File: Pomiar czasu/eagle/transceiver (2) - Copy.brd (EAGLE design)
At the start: 228.6 x 62.2 mm, 126 parts, among them IC1 MEGA8-AI, IC2 LF33, IC3 LF50, IC4 MEGA8-AI, IC5 LF33, IC6 LF50, U1 RFM69HW, U2 RFM69HW

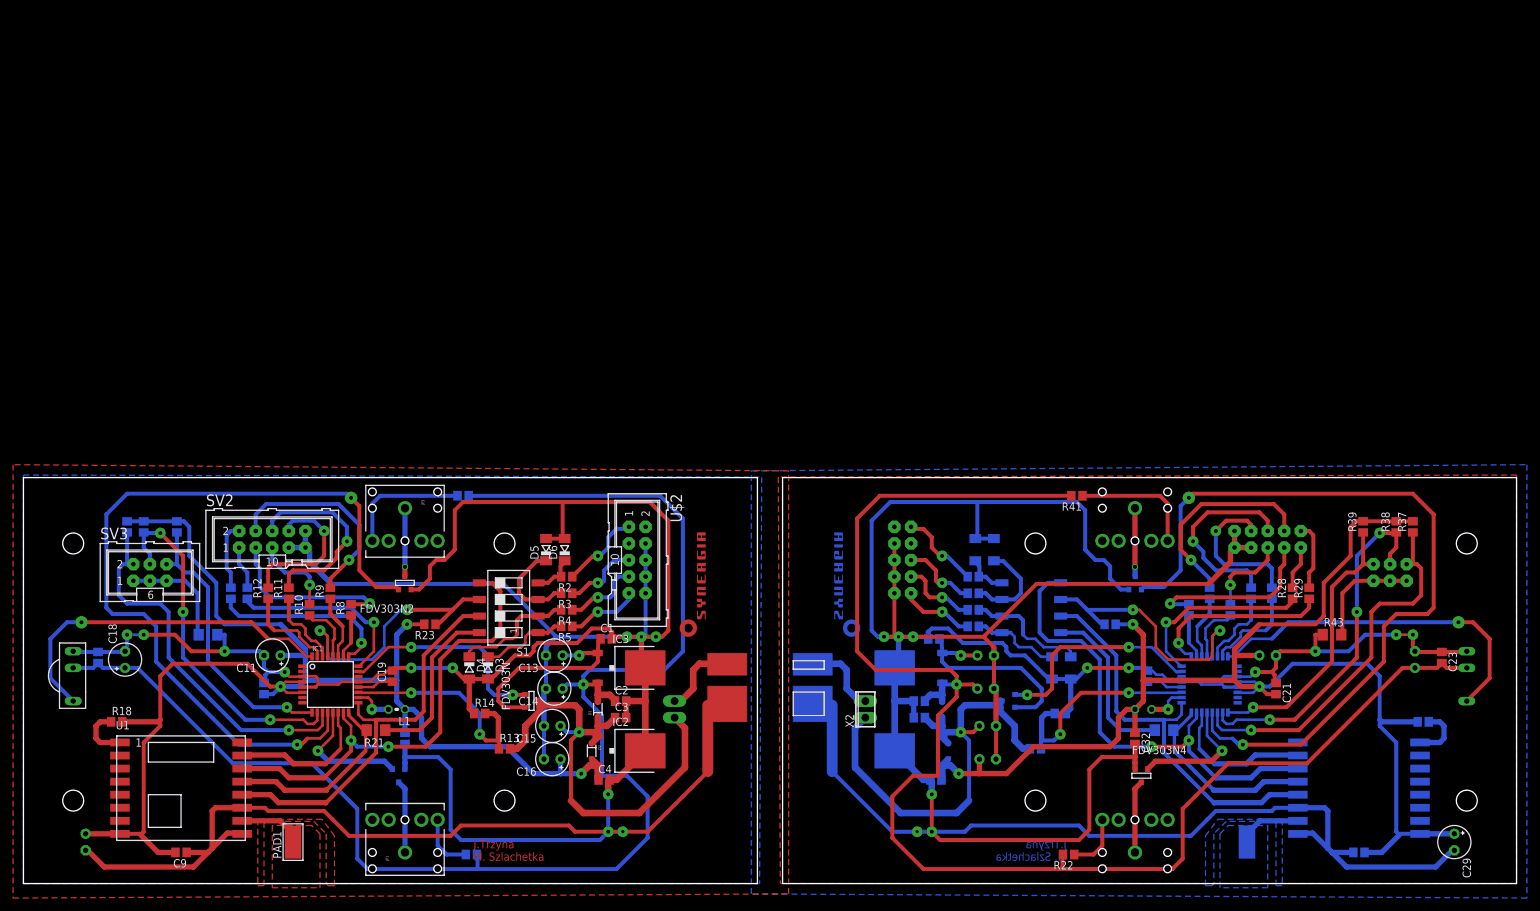
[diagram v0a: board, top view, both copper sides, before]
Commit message: RFM69:communication master->sensor works!
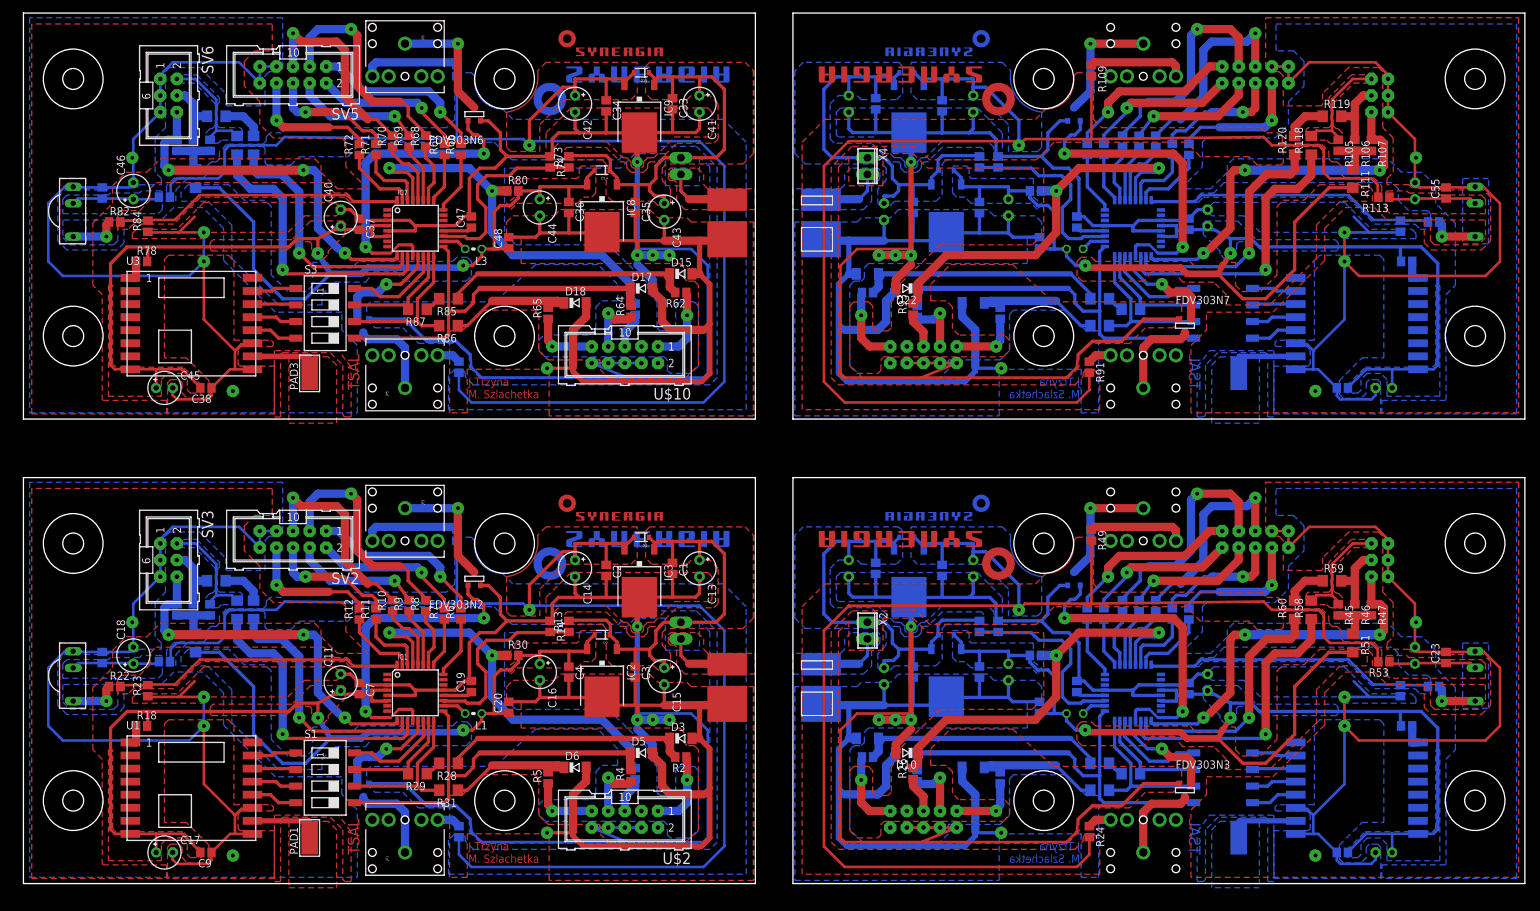
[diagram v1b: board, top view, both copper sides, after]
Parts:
- removed FDV303N: (no value), zetex:SOT-23
- added C33, C34, C35, C36, C37, C38, C39, C47, C48, C49, C50, C51, C52, C53, C54, C55, C63, C64: 100n, resistor:C0805
- added C40, C45, C56, C61: 22u, rcl:E2,5-5
- added C41, C42, C43, C44, C57, C58, C59, C60: 47u, rcl:E2,5-5
- added C46, C62: 4,7u, rcl:E2,5-5
- added D13, D14, D19, D20: BAS16HT1G, SparkFun:SOD-323
- added D15, D16, D17, D18, D21, D22, D23, D24: (no value), diode:SOD80C
- added FDV303N6, FDV303N7, FDV303N8: (no value), zetex:SOT-23
- added IC10, IC7: MEGA8-AI, atmel:TQFP32-08
- added IC11, IC8: LF33, linear:TO252
- added IC12, IC9: LF50, linear:TO252
- added JP5, JP6, JP7, JP8: (no value), SparkFun-Connectors:AUDIO-JACK
- added L3, L4: (no value), resistor:0204V
- added PAD3, PAD4: WIREPADSMD5-2,5, wirepad:5-2,5
- added R100, R102, R66, R67, R68, R69, R70, R72, R96, R97, R98, R99: 1.2k, resistor:R0805
- added R101, R71: 1,2k, resistor:R0805
- added R103, R105, R106, R107, R108, R110, R45, R46, R47, R48, R50, R73, R75, R76, R77, R78, R80: 10k, resistor:R0805
- added R104, R74: 3,6k, resistor:R0805
- added R109, R49, R79: (no value), resistor:R0805
- added R111, R115, R116, R117, R118, R119, R120, R51, R55, R56, R57, R58, R59, R60, R81, R85, R86, R87, R88, R89, R90: 0R, rcl:R1206
- added R112, R52, R62, R63, R64, R65, R82, R92, R93, R94, R95: 330k, resistor:R0805
- added R113, R53, R83: 220R, resistor:R0805
- added R114, R54, R84: 820k, resistor:R0805
- added R61, R91: 36,5R, resistor:R0805
- added S3, S4: SWS004, smd-special:SMS-004
- added SV5, SV7, U$10, U$14: (no value), con-harting-ml:ML10
- added SV6, SV8: (no value), con-harting-ml:ML6
- added TSOP2, TSOP3: TSOP1736, tsop:TSOP17XX
- added U$11, U$15, U$7: (no value), synergia_logo:SYNERGIA_16MM
- added U$12, U$16, U$8: (no value), synergia_logo:SYNERGIA_30MM
- added U$13, U$9: DEANS.MALE, bt_electromech:DEANSM
- added U3, U4: RFM69HW, SparkFun-RF:RFM69W-XXXS2
- added X3, X4: (no value), con-phoenix-254:2POL254
- C1, C10, C12, C19, C2, C20, C21, C22, C23, C3, C31, C32, C4, C5, C6, C7, C8, C9: value (none) -> 100n
- C11, C17, C24, C29: value (none) -> 22u
- C13, C14, C15, C16, C25, C26, C27, C28: value (none) -> 47u
- C18, C30: value (none) -> 4,7u
- D11, D12: value BAS16HT1G -> (none); device SparkFun:SOD-323 -> diode:SOD80C
- D7, D8: value (none) -> BAS16HT1G; device diode:SOD80C -> SparkFun:SOD-323
- R2, R25, R26, R27, R3, R4, R5: value (none) -> 330k
- R21: value 0R -> 220R; device rcl:R1206 -> resistor:R0805
- R22: value 36,5R -> 330k
- R23: value 1k -> 820k
- R24: value (none) -> 36,5R
- R28, R29, R31, R32: value 1.2k -> 0R; device resistor:R0805 -> rcl:R1206
- R30: value 1.2k -> 10k
- R33: value 1,2k -> 0R; device resistor:R0805 -> rcl:R1206
- R34: value 1.2k -> 330k
- R35: value 10k -> 0R; device resistor:R0805 -> rcl:R1206
- R36: value 3,6k -> 1.2k
- R37, R38, R39, R40: value 10k -> 1.2k
- R41: value (none) -> 1,2k
- R42: value 1k -> 1.2k
- R43: value 0R -> 10k; device rcl:R1206 -> resistor:R0805
- R44: value 0R -> 3,6k; device rcl:R1206 -> resistor:R0805
- U$4: value DEANS.MALE -> (none); device bt_electromech:DEANSM -> synergia_logo:SYNERGIA_30MM
- U$5: value (none) -> DEANS.MALE; device con-harting-ml:ML10 -> bt_electromech:DEANSM
- U$6: device synergia_logo:SYNERGIA_16MM -> con-harting-ml:ML10
- moved R33 158.4 mm to (29.5, 43.8), turned to 0 degrees
- moved R32 152.1 mm to (32.7, 39.4)
- moved R22 148.3 mm to (14.0, 27.6), turned to 0 degrees
- moved R29 139.3 mm to (60.3, 14.3), turned to 180 degrees
- moved R28 131.8 mm to (65.1, 15.9), turned to 180 degrees
- moved FDV303N5 124.5 mm to (52.1, 82.9), turned to 0 degrees
- moved R35 121.6 mm to (35.2, 39.4), turned to 90 degrees
- moved R31 120.4 mm to (65.1, 11.7), flipped to the top, turned to 180 degrees
- moved R30 103.7 mm to (74.9, 32.4), flipped to the top, turned to 0 degrees
- moved R43 54.0 mm to (146.4, 36.8), flipped to the bottom, turned to 90 degrees
- moved R34 50.3 mm to (149.5, 13.7)
- moved R37 49.2 mm to (165.4, 38.7), flipped to the bottom
- moved U$4 48.3 mm to (78.1, 51.4)
- moved R40 44.7 mm to (173.4, 40.0), turned to 90 degrees
- moved R23 44.4 mm to (19.1, 27.0), turned to 90 degrees
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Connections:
- removed net 5V_ENABLE: FDV303N.3, IC1.23
- removed net 5V_ENABLE1: FDV303N3.3, IC4.23
- removed net N$34: R27.1, U$5.9
- removed net N$43 (its old number): R31.2, SV1.4
- removed net N$44 (its old number): R32.2, SV1.5
- removed net N$45 (its old number): R33.2, SV1.6
- removed net N$53: JP2.TIP, R22.1
- new net +3V2: C36.1, C37.2, C38.2, C40.+, C44.+, C45.+, C48.1, D14.2, IC7.4, IC7.6, IC8.2, L3.1, R78.2, R80.2, R81.2, U3.8
- new net +3V4: C52.1, C53.2, C54.2, C56.+, C60.+, C61.+, C64.1, D20.2, IC10.4, IC10.6, IC11.2, L4.1, R108.2, R110.2, R111.2, U4.8
- new net +5V2: C34.1, C42.+, D13.2, IC9.2, R61.2, R79.2, R83.2
- new net +5V3: C50.1, C58.+, D19.2, IC12.2, R109.2, R113.2, R91.2
- new net ADC2: IC7.19, R73.1, R74.2
- new net ADC3: IC10.19, R103.1, R104.2
- new net GND2: C33.2, C34.2, C35.2, C36.2, C37.1, C38.1, C39.2, C40.-, C41.-, C42.-, C43.-, C44.-, C45.-, C46.-, C47.2, C48.2, D15.A, D16.A, D17.A, D18.A, FDV303N5.2, FDV303N6.2, IC7.21, IC7.3, IC7.5, IC8.3, IC9.3, R74.1, R84.1, SV5.10, SV5.7, SV5.9, SV6.1, SV6.3, SV6.5, TSOP2.GND, U$10.10, U$10.4, U$10.6, U$10.8, U$9.P$NEG, U3.11, U3.9
- new net GND3: C49.2, C50.2, C51.2, C52.2, C53.1, C54.1, C55.2, C56.-, C57.-, C58.-, C59.-, C60.-, C61.-, C62.-, C63.2, C64.2, D21.A, D22.A, D23.A, D24.A, FDV303N7.2, FDV303N8.2, IC10.21, IC10.3, IC10.5, IC11.3, IC12.3, R104.1, R114.1, SV7.10, SV7.7, SV7.9, SV8.1, SV8.3, SV8.5, TSOP3.GND, U$13.P$NEG, U$14.10, U$14.4, U$14.6, U$14.8, U4.11, U4.9
- new net LED11: IC7.24, R66.1
- new net LED12: IC7.25, R67.1
- new net LED13: IC7.26, R68.1
- new net LED14: IC7.27, R69.1
- new net LED15: IC7.28, R70.1
- new net LED16: IC10.24, R96.1
- new net LED17: IC10.25, R97.1
- new net LED18: IC10.26, R98.1
- new net LED19: IC10.27, R99.1
- new net LED20: IC10.28, R100.1
- new net LED_BATT_GR2: IC7.30, R71.1
- new net LED_BATT_GR3: IC10.30, R101.1
- new net LED_BATT_RED2: IC7.31, R72.1
- new net LED_BATT_RED3: IC10.31, R102.1
- new net LED_STRIPE2: FDV303N6.3, IC7.12
- new net LED_STRIPE3: FDV303N8.3, IC10.12
- new net MISO2: IC7.16, R86.2, S3.6
- new net MISO3: IC10.16, R116.2, S4.6
- new net MOSI2: IC7.15, R87.2, S3.7
- new net MOSI3: IC10.15, R117.2, S4.7
- new net N$100: R85.2, R87.1
- new net N$101: R75.1, R88.2, SV6.2
- new net N$102: R76.1, R89.2, SV6.4
- new net N$103: R89.1, R90.2
- new net N$105: S3.1, U3.15
- new net N$106: S3.2, U3.14
- new net N$107: S3.3, U3.13
- new net N$108: S3.4, U3.12
- new net N$109: R92.1, U$14.1
- new net N$110: R93.1, U$14.5
- new net N$111: R94.1, U$14.7
- new net N$112: R95.1, U$14.9
- new net N$113: R108.1, U4.1
- new net N$114: C49.1, C51.1, C57.+, C59.+, D19.1, D20.1, IC11.1, IC12.1, R103.2, X4.1
- new net N$115: IC10.18, L4.2
- new net N$116: C63.1, IC10.20
- new net N$117: PAD4.1, U4.10
- new net N$118: R96.2, SV7.1
- new net N$119: R97.2, SV7.2
- new net N$120: R98.2, SV7.3
- new net N$121: R99.2, SV7.4
- new net N$122: R100.2, SV7.5
- new net N$123: R101.2, SV7.6
- new net N$124: R102.2, SV7.8
- new net N$126: U$13.P$POS, X4.2
- new net N$127: JP7.TIP, R91.1
- new net N$128: FDV303N7.1, JP7.SLEEVE
- new net N$129: FDV303N8.1, JP8.SLEEVE
- new net N$130: JP8.TIP, R109.1
- new net N$131: R112.1, TSOP3.OUT
- new net N$132: C55.1, C62.+, R113.1, TSOP3.V+
- new net N$133: R105.2, R106.2, R107.2, R111.1
- new net N$134: D21.C, R115.1, R92.2
- new net N$135: D24.C, R116.1, R95.2
- new net N$136: R115.2, R117.1
- new net N$137: R105.1, R118.2, SV8.2
- new net N$138: R106.1, R119.2, SV8.4
- new net N$139: R119.1, R120.2
- new net N$141: S4.1, U4.15
- new net N$142: S4.2, U4.14
- new net N$143: S4.3, U4.13
- new net N$144: S4.4, U4.12
- new net N$37: S1.2, U1.14
- new net N$38: S1.4, U1.12
- new net N$39: S1.1, U1.15
- new net N$51: R41.2, SV1.6
- new net N$59: R52.1, TSOP1.OUT
- new net N$60: C23.1, C30.+, R53.1, TSOP1.V+
- new net N$61: R45.2, R46.2, R47.2, R51.1
- new net N$62: D9.C, R25.2, R55.1
- new net N$63: D12.C, R34.2, R56.1
- new net N$64: R55.2, R57.1
- new net N$65: R45.1, R58.2, SV4.2
- new net N$66: R46.1, R59.2, SV4.4
- new net N$67: R59.1, R60.2
- new net N$69: S2.1, U2.15
- new net N$70: S2.2, U2.14
- new net N$71: S2.3, U2.13
- new net N$72: S2.4, U2.12
- new net N$73: R62.1, U$10.1
- new net N$74: R63.1, U$10.5
- new net N$75: R64.1, U$10.7
- new net N$76: R65.1, U$10.9
- new net N$77: R78.1, U3.1
- new net N$78: C33.1, C35.1, C41.+, C43.+, D13.1, D14.1, IC8.1, IC9.1, R73.2, X3.1
- new net N$79: IC7.18, L3.2
- new net N$80: C47.1, IC7.20
- new net N$81: PAD3.1, U3.10
- new net N$82: R66.2, SV5.1
- new net N$83: R67.2, SV5.2
- new net N$84: R68.2, SV5.3
- new net N$85: R69.2, SV5.4
- new net N$86: R70.2, SV5.5
- new net N$87: R71.2, SV5.6
- new net N$88: R72.2, SV5.8
- new net N$90: U$9.P$POS, X3.2
- new net N$91: JP5.TIP, R61.1
- new net N$92: FDV303N5.1, JP5.SLEEVE
- new net N$93: FDV303N6.1, JP6.SLEEVE
- new net N$94: JP6.TIP, R79.1
- new net N$95: R82.1, TSOP2.OUT
- new net N$96: C39.1, C46.+, R83.1, TSOP2.V+
- new net N$97: R75.2, R76.2, R77.2, R81.1
- new net N$98: D15.C, R62.2, R85.1
- new net N$99: D18.C, R65.2, R86.1
- new net RESET2: D16.C, IC7.29, R63.2, R80.1
- new net RESET3: D22.C, IC10.29, R110.1, R93.2
- new net SCK2: D17.C, IC7.17, R64.2, S3.5
- new net SCK3: D23.C, IC10.17, R94.2, S4.5
- new net SS2: IC7.14, S3.8
- new net SS3: IC10.14, S4.8
- new net SWITCH_DOWN2: IC7.11, R88.1
- new net SWITCH_DOWN3: IC10.11, R118.1
- new net SWITCH_OK2: IC7.10, R90.1
- new net SWITCH_OK3: IC10.10, R120.1
- new net SWITCH_UP2: IC7.9, R77.1, SV6.6
- new net SWITCH_UP3: IC10.9, R107.1, SV8.6
- new net TSAL_ENABLE2: FDV303N5.3, IC7.13
- new net TSAL_ENABLE3: FDV303N7.3, IC10.13
- new net TSOP_OUT2: IC7.32, R82.2, R84.2
- new net TSOP_OUT3: IC10.32, R112.2, R114.2
- net +3V1: now also D8.2, R48.2, R50.2, R51.2; no longer D12.2, R37.2, R38.2, R39.2, R40.2, R42.2
- net +3V3: now also R20.2, R30.2; no longer R15.2, R16.2, R17.2, R23.2
- net +5V: now also R21.2; no longer C10.2, C18.+, TSOP.V+
- net +5V1: now also D7.2, R24.2, R49.2, R53.2; no longer C23.2, C30.+, D11.2, R22.2, R41.2, TSOP1.V+
- net ADC1: now also R43.1, R44.2; no longer R35.1, R36.2
- net GND: now also C10.2, R23.1, SV3.1, SV3.3, SV3.5; no longer C10.1, R20.1
- net GND1: now also C23.2, D11.A, D12.A, FDV303N3.2, R44.1, R54.1, SV4.1, SV4.3, SV4.5, U$5.P$NEG, U$6.10, U$6.4, U$6.6, U$6.8; no longer C23.1, D7.A, D8.A, FDV303N5.2, R36.1, R43.1, U$4.P$NEG, U$5.10, U$5.4, U$5.6, U$5.8
- net LED10: now also R40.1; no longer R32.1
- net LED6: now also R36.1; no longer R28.1
- net LED7: now also R37.1; no longer R29.1
- net LED8: now also R38.1; no longer R30.1
- net LED9: now also R39.1; no longer R31.1
- net LED_BATT_GR1: now also R41.1; no longer R33.1
- net LED_BATT_RED1: now also R42.1; no longer R34.1
- net LED_STRIPE1: now also FDV303N4.3; no longer FDV303N5.3
- net MISO: now also R31.2, S1.6; no longer R21.2, U1.13
- net MISO1: now also R56.2, S2.6; no longer R44.2, U2.13
- net MOSI: now also R29.2, S1.7; no longer S1.5, U1.14
- net MOSI1: now also R57.2, S2.7; no longer S2.5, U2.14
- net N$1: now also R22.1, TSOP.OUT; no longer C1.1, C13.+, FDV303N.2, IC3.1
- net N$22: now also R26.1, U$6.5; no longer R24.1, U$5.1
- net N$23: now also R15.2, R16.2, R17.2, R20.1; no longer R20.2, SV3.1, SV3.3, SV3.5
- net N$24: now also R27.1, U$6.7; no longer R21.1, S1.8
- net N$25: now also C10.1, C18.+, R21.1, TSOP.V+; no longer R25.1, U$5.5
- net N$27: now also C1.1, C13.+, IC3.1; no longer FDV303N.1
- net N$29: now also R28.2, R29.1; no longer D6.C, R2.2, S1.4
- net N$3: now also R25.1, U$6.1; no longer C25.+, C5.1, FDV303N3.2, IC6.1
- net N$30: now also D3.C, R2.2, R28.1; no longer D5.C, R3.2, S1.3
- net N$31: now also D6.C, R31.1, R5.2; no longer D4.C, R4.2, S1.2
- net N$32: now also R15.1, R32.2, SV3.2; no longer D3.C, R5.2, S1.1
- net N$33: now also R16.1, R33.2, SV3.4; no longer R26.1, U$5.7
- net N$35: now also R33.1, R35.2; no longer R40.1, U2.1
- net N$36: now also S1.3, U1.13; no longer C27.+, C8.1, D11.1, D12.1, FDV303N3.1, IC5.1, R35.2, X2.1
- net N$40: now also R34.1, U$6.9; no longer R28.2, SV1.1
- net N$41: now also R48.1, U2.1; no longer R29.2, SV1.2
- net N$42: now also C25.+, C27.+, C5.1, C8.1, D7.1, D8.1, IC5.1, IC6.1, R43.2, X2.1; no longer R30.2, SV1.3
- net N$46: now also R36.2, SV1.1; no longer R34.2, SV1.8
- net N$47: now also R37.2, SV1.2; no longer D8.C, R24.2, S2.4
- net N$48: now also R38.2, SV1.3; no longer D7.C, R25.2, S2.3
- net N$49: now also R39.2, SV1.4; no longer D10.C, R26.2, S2.2
- net N$50: now also R40.2, SV1.5; no longer D9.C, R27.2, S2.1
- net N$52: now also R42.2, SV1.8; no longer U$4.P$POS, X2.2
- net N$54: now also U$5.P$POS, X2.2; no longer FDV303N4.1, JP2.SLEEVE
- net N$55: now also JP2.TIP, R24.1; no longer FDV303N5.1, JP4.SLEEVE
- net N$56: now also FDV303N3.1, JP2.SLEEVE; no longer JP4.TIP, R41.1
- net N$57: now also FDV303N4.1, JP4.SLEEVE; no longer R43.2, SV4.1, SV4.3, SV4.5
- net N$58: now also JP4.TIP, R49.1; no longer R44.1, S2.8
- net RESET: now also D4.C, R3.2, R30.1; no longer R23.1, S1.6
- net RESET1: now also D10.C, R26.2, R50.1; no longer R42.1, S2.6
- net SCK: now also D5.C, R4.2, S1.5; no longer S1.7, U1.12
- net SCK1: now also D11.C, R27.2, S2.5; no longer S2.7, U2.12
- net SS: now also S1.8; no longer U1.15
- net SS1: now also S2.8; no longer U2.15
- net SWITCH_DOWN: now also R32.1; no longer R15.1, SV3.2
- net SWITCH_DOWN1: now also R58.1; no longer R37.1, SV4.2
- net SWITCH_OK: now also R35.1; no longer R16.1, SV3.4
- net SWITCH_OK1: now also R60.1; no longer R38.1, SV4.4
- net SWITCH_UP1: now also R47.1; no longer R39.1
- net TSAL_ENABLE1: now also FDV303N3.3; no longer FDV303N4.3
- net TSOP_OUT: now also R22.2, R23.2; no longer TSOP.OUT
- net TSOP_OUT1: now also R52.2, R54.2; no longer TSOP1.OUT
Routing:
- net GND2: track 0.00 -> 489.9 mm, vias 0 -> 9
- net GND3: track 0.00 -> 489.9 mm, vias 0 -> 9
- net +5V2: track 0.00 -> 212.4 mm, vias 0 -> 1
- net +5V3: track 0.00 -> 212.4 mm, vias 0 -> 1
- net +3V4: track 0.00 -> 184.0 mm, vias 0 -> 2
- net +3V2: track 0.00 -> 184.0 mm, vias 0 -> 2
- net LED_STRIPE1: track 121.6 -> 47.7 mm
- net LED_STRIPE: track 121.6 -> 47.7 mm
- net N$78: track 0.00 -> 68.1 mm
- net N$114: track 0.00 -> 68.1 mm
- net N$36: track 74.6 -> 6.92 mm, vias 1 -> 0
- net RESET3: track 0.00 -> 61.3 mm, vias 0 -> 2
- net RESET2: track 0.00 -> 61.3 mm, vias 0 -> 2
- net SCK3: track 0.00 -> 61.1 mm
- net SCK2: track 0.00 -> 61.1 mm
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- added copper zone on layer 1, net +3V1
- added copper zone on layer 16, net +3V1
- added copper zone on layer 1, net +3V2
- added copper zone on layer 16, net +3V2
- added copper zone on layer 1, net +3V3
- added copper zone on layer 16, net +3V3
- added copper zone on layer 1, net +3V4
- added copper zone on layer 16, net +3V4
- added copper zone on layer 1, net +5V
- added copper zone on layer 16, net +5V
- added copper zone on layer 1, net +5V1
- added copper zone on layer 16, net +5V1
- added copper zone on layer 1, net +5V2
- added copper zone on layer 16, net +5V2
- added copper zone on layer 1, net +5V3
- added copper zone on layer 16, net +5V3
- added copper zone on layer 1, net GND2
- added copper zone on layer 16, net GND2
- added copper zone on layer 1, net GND3
- added copper zone on layer 16, net GND3
- added copper zone on layer 16, net N$1
- added copper zone on layer 16, net N$101
- added copper zone on layer 1, net N$104
- added copper zone on layer 16, net N$114
- added copper zone on layer 16, net N$117
- added copper zone on layer 16, net N$125
- added copper zone on layer 16, net N$126
- added copper zone on layer 1, net N$131
- added copper zone on layer 1, net N$132
- added copper zone on layer 1, net N$137
- added copper zone on layer 16, net N$140
- added copper zone on layer 1, net N$19
- added copper zone on layer 16, net N$25
- added copper zone on layer 1, net N$27
- added copper zone on layer 16, net N$32
- added copper zone on layer 1, net N$34
- added copper zone on layer 16, net N$42
- added copper zone on layer 16, net N$53
- added copper zone on layer 16, net N$54
- added copper zone on layer 1, net N$59
- added copper zone on layer 1, net N$60
- added copper zone on layer 1, net N$65
- added copper zone on layer 16, net N$68
- added copper zone on layer 1, net N$78
- added copper zone on layer 1, net N$81
- added copper zone on layer 1, net N$89
- added copper zone on layer 1, net N$90
- added copper zone on layer 16, net N$95
- added copper zone on layer 16, net N$96
- added copper zone on layer 1, net TSOP_OUT
- added copper zone on layer 16, net TSOP_OUT1
- added copper zone on layer 1, net TSOP_OUT2
- added copper zone on layer 16, net TSOP_OUT3
- removed copper zone on layer 16, net N$51
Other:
- board size 228.6 x 62.2 mm -> 229.9 x 133.3 mm
- board text added: "TSAL"

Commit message: Channel: 442MHz(!!), ping with acknowledgement
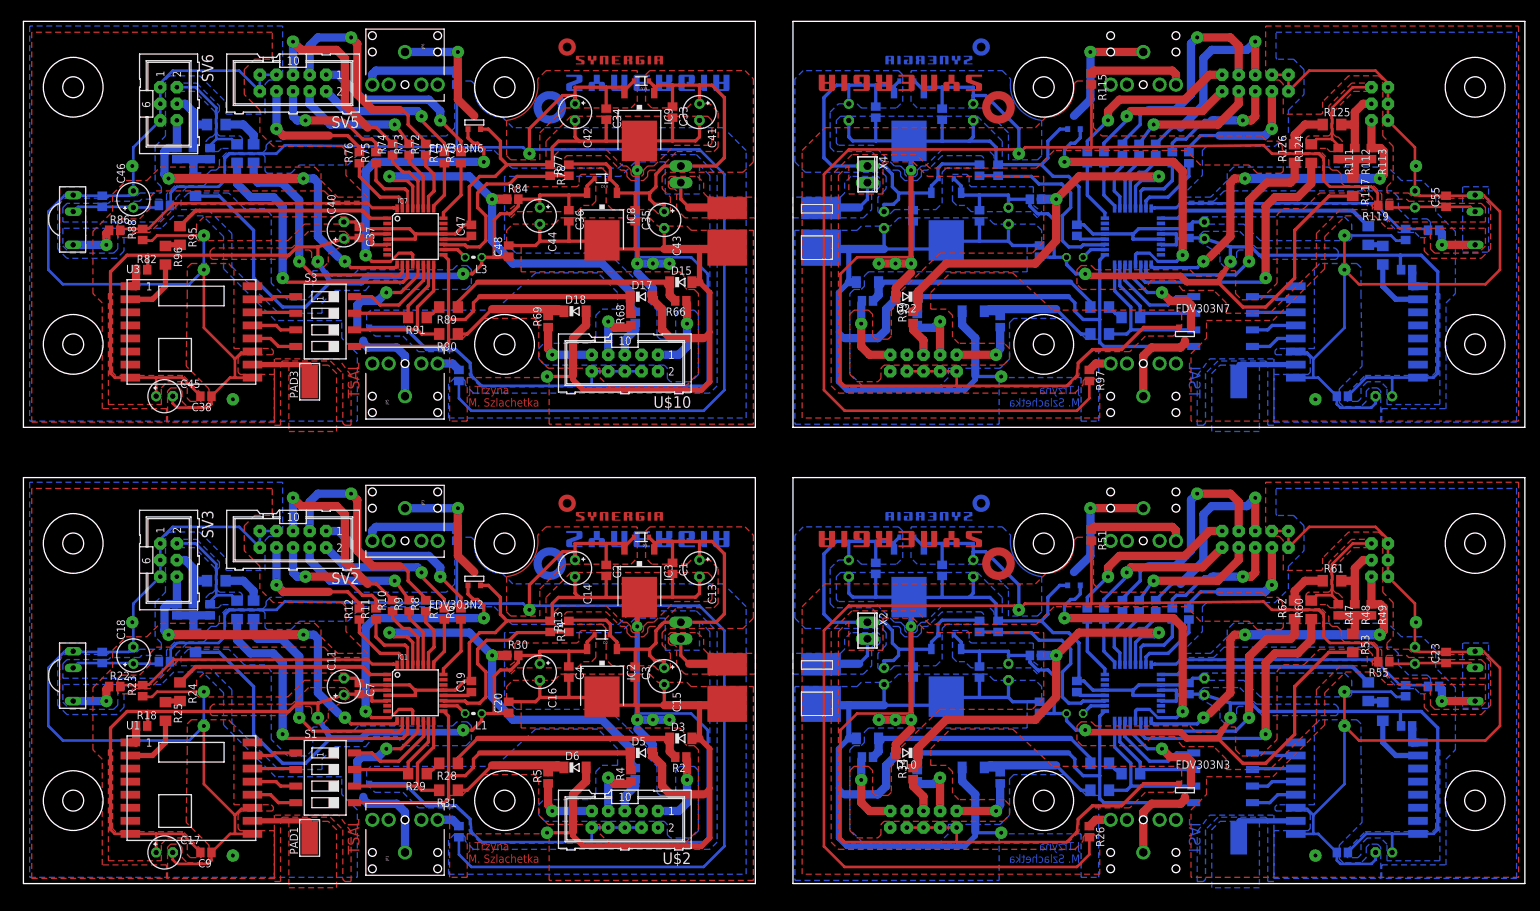
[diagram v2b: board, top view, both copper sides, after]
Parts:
- added R121, R122, R123, R124, R125, R126, R127, R128: 0R, rcl:R1206
- R100, R36, R37, R66, R67, R68, R69, R98, R99: value 1.2k -> 330k
- R101: value 1,2k -> 330k
- R103, R105, R106, R108, R73, R76: value 10k -> 1.2k
- R104, R44, R74: value 3,6k -> 1.2k
- R107, R43, R75: value 10k -> 1,2k
- R109, R49, R79: value (none) -> 10k
- R110, R46, R78: value 10k -> 3,6k
- R111, R116, R81: value 0R -> 10k; device rcl:R1206 -> resistor:R0805
- R112, R52, R82: value 330k -> 10k
- R113: value 220R -> 10k
- R114, R84: value 820k -> 10k
- R115, R51: value 0R -> (none); device rcl:R1206 -> resistor:R0805
- R118, R86: value 0R -> 330k; device rcl:R1206 -> resistor:R0805
- R119, R55, R87: value 0R -> 220R; device rcl:R1206 -> resistor:R0805
- R120, R56, R88: value 0R -> 820k; device rcl:R1206 -> resistor:R0805
- R24, R61, R91: value 36,5R -> 0R; device resistor:R0805 -> rcl:R1206
- R25, R62, R63, R64, R92, R93, R94, R95: value 330k -> 0R; device resistor:R0805 -> rcl:R1206
- R26, R65: value 330k -> 36,5R
- R41, R71: value 1,2k -> 1.2k
- R53: value 220R -> 0R; device resistor:R0805 -> rcl:R1206
- R54: value 820k -> 330k
- R83: value 220R -> (none)
- R96: value 1.2k -> 0R; device resistor:R0805 -> rcl:R1206
- R97: value 1.2k -> 36,5R
- moved R96 142.1 mm to (21.7, 93.7), flipped to the top, turned to 270 degrees
- moved R24 140.9 mm to (24.0, 26.8)
- moved R61 137.6 mm to (200.3, 43.8), flipped to the top, turned to 0 degrees
- moved R64 130.4 mm to (208.1, 23.8), flipped to the bottom, turned to 270 degrees
- moved R63 126.6 mm to (205.9, 26.8), turned to 270 degrees
- moved R95 126.1 mm to (24.0, 96.7), flipped to the top, turned to 270 degrees
- moved R93 110.4 mm to (29.5, 113.7), flipped to the bottom, turned to 0 degrees
- moved R25 107.7 mm to (21.7, 23.8), flipped to the top, turned to 270 degrees
- moved R62 105.8 mm to (194.6, 39.4), turned to 90 degrees
- moved R94 104.4 mm to (35.2, 109.2)
- moved R91 103.2 mm to (60.3, 84.1), turned to 180 degrees
- moved R92 98.8 mm to (32.7, 109.2), turned to 90 degrees
- moved R78 64.1 mm to (80.6, 106.7), turned to 270 degrees
- moved R52 61.1 mm to (154.9, 32.4)
- moved R77 60.1 mm to (83.5, 106.7), flipped to the top, turned to 90 degrees
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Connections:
- removed net N$109 (its old number): R92.1, U$14.1
- removed net N$110 (its old number): R93.1, U$14.5
- removed net N$111 (its old number): R94.1, U$14.7
- removed net N$112 (its old number): R95.1, U$14.9
- removed net N$121 (its old number): R99.2, SV7.4
- removed net N$122 (its old number): R100.2, SV7.5
- removed net N$123 (its old number): R101.2, SV7.6
- removed net N$131: R112.1, TSOP3.OUT
- removed net N$132 (its old number): C55.1, C62.+, R113.1, TSOP3.V+
- removed net N$134 (its old number): D21.C, R115.1, R92.2
- removed net N$135 (its old number): D24.C, R116.1, R95.2
- removed net N$46 (its old number): R36.2, SV1.1
- removed net N$47 (its old number): R37.2, SV1.2
- removed net N$55: JP2.TIP, R24.1
- removed net N$58 (its old number): JP4.TIP, R49.1
- removed net N$59 (its old number): R52.1, TSOP1.OUT
- removed net N$73 (its old number): R62.1, U$10.1
- removed net N$74 (its old number): R63.1, U$10.5
- removed net N$83 (its old number): R67.2, SV5.2
- removed net N$84 (its old number): R68.2, SV5.3
- removed net N$85 (its old number): R69.2, SV5.4
- removed net N$94 (its old number): JP6.TIP, R79.1
- removed net N$96 (its old number): C39.1, C46.+, R83.1, TSOP2.V+
- removed net N$97 (its old number): R75.2, R76.2, R77.2, R81.1
- new net DIO0: IC1.1, R24.1
- new net DIO1: IC4.1, R63.1
- new net DIO2: IC7.1, R95.1
- new net DIO3: IC10.1, R127.1
- new net N$104: R89.2, R91.1
- new net N$105: R79.1, R92.2, SV6.2
- new net N$106: R80.1, R93.2, SV6.4
- new net N$107: R93.1, R94.2
- new net N$115: R98.1, U$14.1
- new net N$116: R99.1, U$14.5
- new net N$117: R100.1, U$14.7
- new net N$125: R103.2, SV7.2
- new net N$126: R104.2, SV7.3
- new net N$128: R106.2, SV7.5
- new net N$129: R107.2, SV7.6
- new net N$140: D21.C, R121.1, R98.2
- new net N$141: D24.C, R101.2, R122.1
- new net N$142: R121.2, R123.1
- new net N$143: R111.1, R124.2, SV8.2
- new net N$144: R112.1, R125.2, SV8.4
- new net N$145: R125.1, R126.2
- new net N$151: R127.2, R128.1
- new net N$152: R128.2, U4.2
- new net N$43: C25.+, C27.+, C5.1, C8.1, D7.1, D8.1, IC5.1, IC6.1, R45.2, X2.1
- new net N$45: R25.2, U1.2
- new net N$53: R43.2, SV1.6
- new net N$54: R44.2, SV1.8
- new net N$57: JP2.TIP, R26.1
- new net N$68: R48.1, R61.2, SV4.4
- new net N$69: R61.1, R62.2
- new net N$79: R68.1, U$10.7
- new net N$80: R69.1, U$10.9
- new net N$81: R82.1, U3.1
- new net N$89: R73.2, SV5.4
- new net N$90: R74.2, SV5.5
- new net N$92: R76.2, SV5.8
- net +3V1: now also R52.2, R53.2; no longer R48.2, R51.2
- net +3V2: now also R82.2, R84.2, R85.2; no longer R78.2, R80.2, R81.2
- net +3V4: now also R114.2, R116.2, R117.2; no longer R108.2, R110.2, R111.2
- net +5V1: now also R26.2, R51.2, R55.2; no longer R24.2, R49.2, R53.2
- net +5V2: now also R65.2, R87.2; no longer R61.2, R79.2
- net +5V3: now also R115.2, R119.2, R97.2; no longer R109.2, R113.2, R91.2
- net ADC1: now also R45.1, R46.2; no longer R43.1, R44.2
- net ADC2: now also R77.1, R78.2; no longer R73.1, R74.2
- net ADC3: now also R109.1, R110.2; no longer R103.1, R104.2
- net GND1: now also R46.1, R56.1; no longer R44.1, R54.1
- net GND2: now also R78.1, R88.1; no longer R74.1, R84.1
- net GND3: now also R110.1, R120.1; no longer R104.1, R114.1
- net LED10: now also R42.1; no longer R40.1
- net LED11: now also R70.1; no longer R66.1
- net LED12: now also R71.1; no longer R67.1
- net LED13: now also R72.1; no longer R68.1
- net LED14: now also R73.1; no longer R69.1
- net LED15: now also R74.1; no longer R70.1
- net LED16: now also R102.1; no longer R96.1
- net LED17: now also R103.1; no longer R97.1
- net LED18: now also R104.1; no longer R98.1
- net LED19: now also R105.1; no longer R99.1
- net LED20: now also R106.1; no longer R100.1
- net LED6: now also R38.1; no longer R36.1
- net LED7: now also R39.1; no longer R37.1
- net LED8: now also R40.1; no longer R38.1
- net LED9: now also R41.1; no longer R39.1
- net LED_BATT_GR1: now also R43.1; no longer R41.1
- net LED_BATT_GR2: now also R75.1; no longer R71.1
- net LED_BATT_GR3: now also R107.1; no longer R101.1
- net LED_BATT_RED1: now also R44.1; no longer R42.1
- net LED_BATT_RED2: now also R76.1; no longer R72.1
- net LED_BATT_RED3: now also R108.1; no longer R102.1
- net MISO1: now also R58.2; no longer R56.2
- net MISO2: now also R90.2; no longer R86.2
- net MISO3: now also R122.2; no longer R116.2
- net MOSI1: now also R59.2; no longer R57.2
- net MOSI2: now also R91.2; no longer R87.2
- net MOSI3: now also R123.2; no longer R117.2
- net N$100: now also C39.1, C46.+, TSOP2.V+; no longer R85.2
- net N$101: now also R79.2, R80.2, R81.2, R85.1; no longer R75.1, R88.2, SV6.2
- net N$102: now also D15.C, R66.2, R89.1; no longer R76.1, R89.2, SV6.4
- net N$103: now also D18.C, R69.2, R90.1; no longer R89.1, R90.2
- net N$113: now also R95.2, R96.1; no longer R108.1, U4.1
- net N$114: now also R96.2, U3.2; no longer C49.1, C51.1, C57.+, C59.+, D19.1, D20.1, IC11.1, IC12.1, R103.2, X4.1
- net N$118: now also R101.1, U$14.9; no longer R96.2, SV7.1
- net N$119: now also R114.1, U4.1; no longer R97.2, SV7.2
- net N$120: now also C49.1, C51.1, C57.+, C59.+, D19.1, D20.1, IC11.1, IC12.1, R109.2, X4.1; no longer R98.2, SV7.3
- net N$124: now also SV7.1; no longer SV7.8
- net N$127: now also R105.2, SV7.4; no longer JP7.TIP, R91.1
- net N$130: now also R108.2, SV7.8; no longer JP8.TIP, R109.1
- net N$133: now also JP7.TIP, R97.1; no longer R105.2, R106.2, R107.2, R111.1
- net N$136: now also JP8.TIP, R115.1; no longer R115.2, R117.1
- net N$137: now also R118.1, TSOP3.OUT; no longer R105.1, R118.2, SV8.2
- net N$138: now also C55.1, C62.+, R119.1, TSOP3.V+; no longer R106.1, R119.2, SV8.4
- net N$139: now also R111.2, R112.2, R113.2, R117.1; no longer R119.1, R120.2
- net N$22: now also R34.1; no longer R26.1
- net N$24: now also R24.2, R25.1; no longer R27.1, U$6.7
- net N$3: now also R27.1; no longer R25.1
- net N$40: now also R36.1, U$6.7; no longer R34.1, U$6.9
- net N$41: now also R37.1, U$6.9; no longer R48.1, U2.1
- net N$42: now also R50.1, U2.1; no longer C25.+, C27.+, C5.1, C8.1, D7.1, D8.1, IC5.1, IC6.1, R43.2, X2.1
- net N$48: now also SV1.1; no longer SV1.3
- net N$49: now also SV1.2; no longer SV1.4
- net N$50: now also SV1.3; no longer SV1.5
- net N$51: now also SV1.4; no longer SV1.6
- net N$52: now also SV1.5; no longer SV1.8
- net N$60: now also JP4.TIP, R51.1; no longer C23.1, C30.+, R53.1, TSOP1.V+
- net N$61: now also R54.1, TSOP1.OUT; no longer R45.2, R46.2, R47.2, R51.1
- net N$62: now also C23.1, C30.+, TSOP1.V+; no longer D9.C, R25.2
- net N$63: now also R47.2, R48.2, R49.2, R53.1; no longer D12.C, R34.2, R56.1
- net N$64: now also D9.C, R27.2; no longer R55.2
- net N$65: now also D12.C, R37.2, R58.1; no longer R45.1, R58.2, SV4.2
- net N$66: now also R57.2, R59.1; no longer R46.1, R59.2, SV4.4
- net N$67: now also R47.1, SV4.2; no longer R59.1
- net N$75: now also R63.2; no longer U$10.7
- net N$76: now also R64.2, U2.2; no longer R65.1, U$10.9
- net N$77: now also R66.1, U$10.1; no longer R78.1, U3.1
- net N$78: now also R67.1, U$10.5; no longer C33.1, C35.1, C41.+, C43.+, D13.1, D14.1, IC8.1, IC9.1, R73.2, X3.1
- net N$82: now also C33.1, C35.1, C41.+, C43.+, D13.1, D14.1, IC8.1, IC9.1, R77.2, X3.1; no longer R66.2, SV5.1
- net N$86: now also SV5.1; no longer SV5.5
- net N$87: now also SV5.2; no longer SV5.6
- net N$88: now also SV5.3; no longer SV5.8
- net N$91: now also R75.2, SV5.6; no longer JP5.TIP, R61.1
- net N$95: now also JP5.TIP, R65.1; no longer R82.1, TSOP2.OUT
- net N$98: now also JP6.TIP, R83.1; no longer D15.C, R62.2, R85.1
- net N$99: now also TSOP2.OUT; no longer D18.C, R65.2
- net RESET1: now also R34.2, R52.1; no longer R26.2, R50.1
- net RESET2: now also R67.2, R84.1; no longer R63.2, R80.1
- net RESET3: now also R116.1, R99.2; no longer R110.1, R93.2
- net SCK1: now also R36.2; no longer R27.2
- net SCK2: now also R68.2; no longer R64.2
- net SCK3: now also R100.2; no longer R94.2
- net SWITCH_DOWN1: now also R60.1; no longer R58.1
- net SWITCH_DOWN2: now also R92.1; no longer R88.1
- net SWITCH_DOWN3: now also R124.1; no longer R118.1
- net SWITCH_OK1: now also R62.1; no longer R60.1
- net SWITCH_OK2: now also R94.1; no longer R90.1
- net SWITCH_OK3: now also R126.1; no longer R120.1
- net SWITCH_UP1: now also R49.1; no longer R47.1
- net SWITCH_UP2: now also R81.1; no longer R77.1
- net SWITCH_UP3: now also R113.1; no longer R107.1
- net TSOP_OUT1: now also R56.2; no longer R52.2
- net TSOP_OUT2: now also R86.2, R88.2; no longer R82.2, R84.2
- net TSOP_OUT3: now also R118.2, R120.2; no longer R112.2, R114.2
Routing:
- net N$43: track 0.00 -> 68.1 mm
- net N$42: track 68.1 -> 3.40 mm
- net N$78: track 68.1 -> 5.52 mm
- net N$114: track 68.1 -> 9.54 mm
- net N$82: track 27.4 -> 68.1 mm, vias 1 -> 0
- net N$134 (its old number): track 38.1 -> 0.00 mm
- net N$140: track 0.00 -> 38.1 mm
- net N$64: track 2.50 -> 38.1 mm
- net N$84 (its old number): track 35.0 -> 0.00 mm, vias 1 -> 0
- net N$126: track 0.00 -> 35.0 mm, vias 0 -> 1
- net DIO1: track 0.00 -> 33.4 mm
- net DIO0: track 0.00 -> 33.4 mm
- net DIO3: track 0.00 -> 33.4 mm
- net DIO2: track 0.00 -> 33.4 mm
- net N$120: track 35.0 -> 68.1 mm, vias 1 -> 0
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- added copper zone on layer 16, net N$100
- added copper zone on layer 16, net N$105
- added copper zone on layer 1, net N$108
- added copper zone on layer 16, net N$120
- added copper zone on layer 16, net N$131
- added copper zone on layer 1, net N$138
- added copper zone on layer 1, net N$143
- added copper zone on layer 16, net N$146
- added copper zone on layer 16, net N$43
- added copper zone on layer 16, net N$55
- added copper zone on layer 1, net N$61
- added copper zone on layer 1, net N$62
- added copper zone on layer 1, net N$67
- added copper zone on layer 16, net N$70
- added copper zone on layer 1, net N$82
- added copper zone on layer 1, net N$93
- added copper zone on layer 16, net N$99
- removed copper zone on layer 16, net N$101
- removed copper zone on layer 1, net N$104
- removed copper zone on layer 16, net N$114
- removed copper zone on layer 16, net N$125
- removed copper zone on layer 1, net N$131
- removed copper zone on layer 1, net N$132 (its old number)
- removed copper zone on layer 16, net N$140
- removed copper zone on layer 16, net N$42
- removed copper zone on layer 16, net N$53
- removed copper zone on layer 1, net N$59 (its old number)
- removed copper zone on layer 1, net N$60
- removed copper zone on layer 1, net N$65
- removed copper zone on layer 16, net N$68
- removed copper zone on layer 1, net N$78
- removed copper zone on layer 1, net N$89
- removed copper zone on layer 16, net N$95
- removed copper zone on layer 16, net N$96 (its old number)
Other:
- board size 229.9 x 133.3 mm -> 229.9 x 132 mm
